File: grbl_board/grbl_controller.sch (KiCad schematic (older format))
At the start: 38 parts, among them J3 USB_B, J4 ICSP, SW1 SW_Push, U1 FT231XS, U2 ATmega2560-16AU, Y1 16M

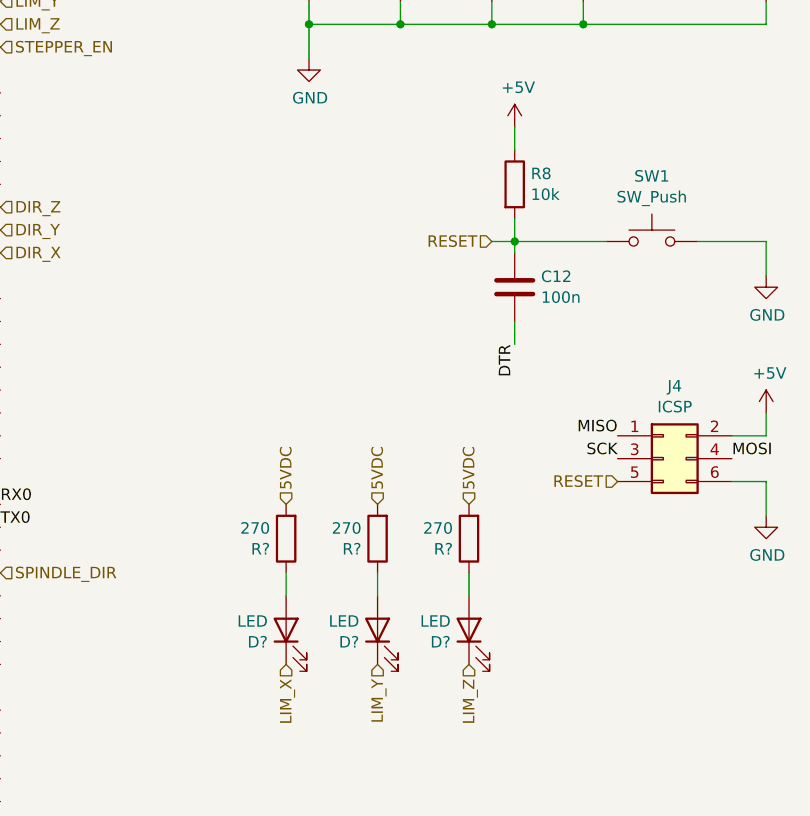
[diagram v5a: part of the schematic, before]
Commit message: updated board with 24V reg
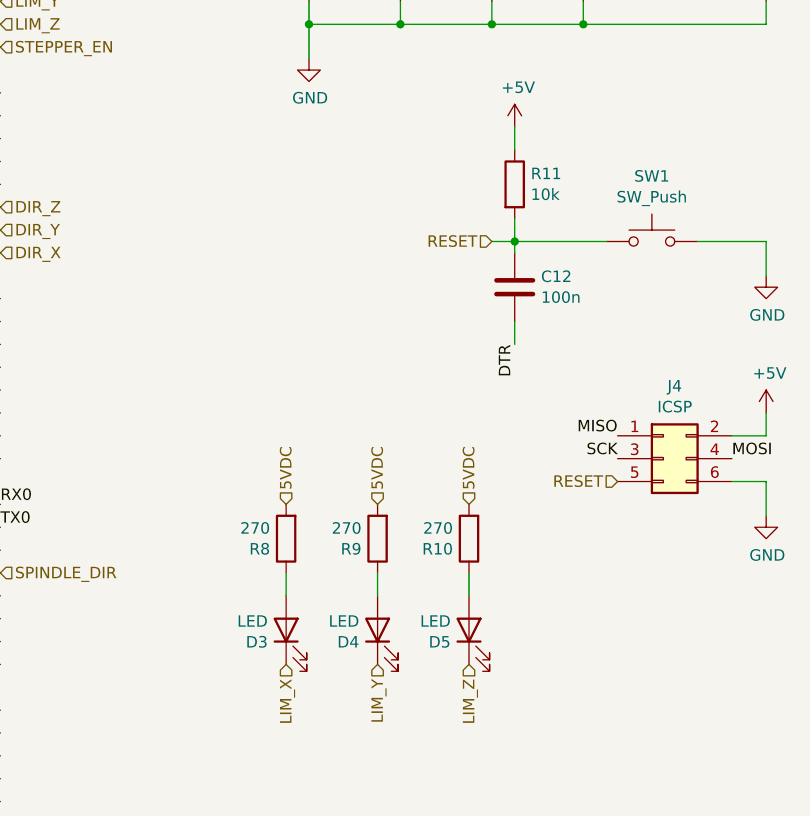
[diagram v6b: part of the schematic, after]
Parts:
- gave numbers to parts that had none: 6
- renumbered R8 to R11
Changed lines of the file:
@@
 $EndComp
 $Comp
-L power:GND #PWR09
+L power:GND #PWR011
 U 1 1 61772314
 P 3100 2100
-F 0 "#PWR09" H 3100 1850 50  0001 C CNN
+F 0 "#PWR011" H 3100 1850 50  0001 C CNN
 F 1 "GND" H 3105 1927 50  0000 C CNN
 F 2 "" H 3100 2100 50  0001 C CNN
@@
 	4700 2000 4700 2150
 $Comp
-L power:GND #PWR011
+L power:GND #PWR012
 U 1 1 6177BB8C
 P 4700 2550
-F 0 "#PWR011" H 4700 2300 50  0001 C CNN
+F 0 "#PWR012" H 4700 2300 50  0001 C CNN
 F 1 "GND" H 4705 2377 50  0000 C CNN
 F 2 "" H 4700 2550 50  0001 C CNN
@@
 	8500 2400 8900 2400
 $Comp
-L power:+5V #PWR014
+L power:+5V #PWR015
 U 1 1 617AAEC0
 P 8100 2300
-F 0 "#PWR014" H 8100 2150 50  0001 C CNN
+F 0 "#PWR015" H 8100 2150 50  0001 C CNN
 F 1 "+5V" H 8115 2473 50  0000 C CNN
 F 2 "" H 8100 2300 50  0001 C CNN
@@
 Connection ~ 8100 2400
 $Comp
-L power:GND #PWR015
+L power:GND #PWR016
 U 1 1 617AC8A9
 P 8100 3050
-F 0 "#PWR015" H 8100 2800 50  0001 C CNN
+F 0 "#PWR016" H 8100 2800 50  0001 C CNN
 F 1 "GND" H 8105 2877 50  0000 C CNN
 F 2 "" H 8100 3050 50  0001 C CNN
@@
 	6050 900  6050 1100
 $Comp
-L power:+5V #PWR012
+L power:+5V #PWR013
 U 1 1 617AFBE7
 P 5800 850
-F 0 "#PWR012" H 5800 700 50  0001 C CNN
+F 0 "#PWR013" H 5800 700 50  0001 C CNN
 F 1 "+5V" H 5815 1023 50  0000 C CNN
 F 2 "" H 5800 850 50  0001 C CNN
@@
 	5950 950  5950 1100
 $Comp
-L power:GND #PWR013
+L power:GND #PWR014
 U 1 1 617B278B
 P 5950 7100
-F 0 "#PWR013" H 5950 6850 50  0001 C CNN
+F 0 "#PWR014" H 5950 6850 50  0001 C CNN
 F 1 "GND" H 5955 6927 50  0000 C CNN
 F 2 "" H 5950 7100 50  0001 C CNN
@@
 SCK
 $Comp
-L power:GND #PWR017
+L power:GND #PWR018
 U 1 1 617C6BF5
 P 10100 4000
-F 0 "#PWR017" H 10100 3750 50  0001 C CNN
+F 0 "#PWR018" H 10100 3750 50  0001 C CNN
 F 1 "GND" H 10105 3827 50  0000 C CNN
 F 2 "" H 10100 4000 50  0001 C CNN
@@
 MISO
 $Comp
-L power:+5V #PWR018
+L power:+5V #PWR019
 U 1 1 617D7EA2
 P 10100 4600
-F 0 "#PWR018" H 10100 4450 50  0001 C CNN
+F 0 "#PWR019" H 10100 4450 50  0001 C CNN
 F 1 "+5V" H 10115 4773 50  0000 C CNN
 F 2 "" H 10100 4600 50  0001 C CNN
@@
 	10100 4700 9950 4700
 $Comp
-L power:GND #PWR019
+L power:GND #PWR020
 U 1 1 617D9FFF
 P 10100 5050
-F 0 "#PWR019" H 10100 4800 50  0001 C CNN
+F 0 "#PWR020" H 10100 4800 50  0001 C CNN
 F 1 "GND" H 10105 4877 50  0000 C CNN
 F 2 "" H 10100 5050 50  0001 C CNN
@@
 	3100 2000 3100 1700
 $Comp
-L power:+5V #PWR016
+L power:+5V #PWR017
 U 1 1 617EF684
 P 9000 3350
-F 0 "#PWR016" H 9000 3200 50  0001 C CNN
+F 0 "#PWR017" H 9000 3200 50  0001 C CNN
 F 1 "+5V" H 9015 3523 50  0000 C CNN
 F 2 "" H 9000 3350 50  0001 C CNN
@@
 	9000 3350 9000 3450
 $Comp
-L Device:R R8
+L Device:R R11
 U 1 1 617F074D
 P 9000 3600
-F 0 "R8" H 9070 3646 50  0000 L CNN
+F 0 "R11" H 9070 3646 50  0000 L CNN
 F 1 "10k" H 9070 3555 50  0000 L CNN
 F 2 "Resistor_SMD:R_0805_2012Metric_Pad1.15x1.40mm_HandSolder" V 8930 3600 50  0001 C CNN
@@
 	1550 6650 1550 6600
 $Comp
-L power:GND #PWR07
+L power:GND #PWR08
 U 1 1 61866176
 P 1150 6700
-F 0 "#PWR07" H 1150 6450 50  0001 C CNN
+F 0 "#PWR08" H 1150 6450 50  0001 C CNN
 F 1 "GND" H 1155 6527 50  0000 C CNN
 F 2 "" H 1150 6700 50  0001 C CNN
@@
 	1000 4550 1000 4400
 $Comp
-L power:GND #PWR06
+L power:GND #PWR07
 U 1 1 618A6872
 P 1000 4550
-F 0 "#PWR06" H 1000 4300 50  0001 C CNN
+F 0 "#PWR07" H 1000 4300 50  0001 C CNN
 F 1 "GND" H 1005 4377 50  0000 C CNN
 F 2 "" H 1000 4550 50  0001 C CNN
@@
 	1550 5850 1550 5900
 $Comp
-L power:GND #PWR08
+L power:GND #PWR09
 U 1 1 61898861
 P 1550 5900
-F 0 "#PWR08" H 1550 5650 50  0001 C CNN
+F 0 "#PWR09" H 1550 5650 50  0001 C CNN
 F 1 "GND" H 1555 5727 50  0000 C CNN
 F 2 "" H 1550 5900 50  0001 C CNN
@@
 AR Path="/619755E7/61CDF7A9" Ref="D?"  Part="1"
 AR Path="/61D39570/61CDF7A9" Ref="D?"  Part="1"
-F 0 "D?" V 8747 5630 50  0000 L CNN
+AR Path="/61764DEB/61CDF7A9" Ref="D5"  Part="1"
+F 0 "D5" V 8747 5630 50  0000 L CNN
 F 1 "LED" V 8838 5630 50  0000 L CNN
 F 2 "LED_SMD:LED_1206_3216Metric_Pad1.42x1.75mm_HandSolder" H 8800 5550 50  0001 C CNN
@@
 AR Path="/619755E7/61CDF7B0" Ref="R?"  Part="1"
 AR Path="/61D39570/61CDF7B0" Ref="R?"  Part="1"
-F 0 "R?" H 8870 5196 50  0000 L CNN
+AR Path="/61764DEB/61CDF7B0" Ref="R10"  Part="1"
+F 0 "R10" H 8870 5196 50  0000 L CNN
 F 1 "270" H 8870 5105 50  0000 L CNN
 F 2 "Resistor_SMD:R_0805_2012Metric_Pad1.15x1.40mm_HandSolder" V 8730 5150 50  0001 C CNN
@@
 AR Path="/619755E7/61CDF7B9" Ref="D?"  Part="1"
 AR Path="/61D39570/61CDF7B9" Ref="D?"  Part="1"
-F 0 "D?" V 8347 5630 50  0000 L CNN
+AR Path="/61764DEB/61CDF7B9" Ref="D4"  Part="1"
+F 0 "D4" V 8347 5630 50  0000 L CNN
 F 1 "LED" V 8438 5630 50  0000 L CNN
 F 2 "LED_SMD:LED_1206_3216Metric_Pad1.42x1.75mm_HandSolder" H 8400 5550 50  0001 C CNN
@@
 AR Path="/619755E7/61CDF7C0" Ref="R?"  Part="1"
 AR Path="/61D39570/61CDF7C0" Ref="R?"  Part="1"
-F 0 "R?" H 8470 5196 50  0000 L CNN
+AR Path="/61764DEB/61CDF7C0" Ref="R9"  Part="1"
+F 0 "R9" H 8470 5196 50  0000 L CNN
 F 1 "270" H 8470 5105 50  0000 L CNN
 F 2 "Resistor_SMD:R_0805_2012Metric_Pad1.15x1.40mm_HandSolder" V 8330 5150 50  0001 C CNN
@@
 AR Path="/619755E7/61CDF7C9" Ref="R?"  Part="1"
 AR Path="/61D39570/61CDF7C9" Ref="R?"  Part="1"
-F 0 "R?" H 8070 5196 50  0000 L CNN
+AR Path="/61764DEB/61CDF7C9" Ref="R8"  Part="1"
+F 0 "R8" H 8070 5196 50  0000 L CNN
 F 1 "270" H 8070 5105 50  0000 L CNN
 F 2 "Resistor_SMD:R_0805_2012Metric_Pad1.15x1.40mm_HandSolder" V 7930 5150 50  0001 C CNN
@@
 AR Path="/619755E7/61CDF7D0" Ref="D?"  Part="1"
 AR Path="/61D39570/61CDF7D0" Ref="D?"  Part="1"
-F 0 "D?" V 7947 5630 50  0000 L CNN
+AR Path="/61764DEB/61CDF7D0" Ref="D3"  Part="1"
+F 0 "D3" V 7947 5630 50  0000 L CNN
 F 1 "LED" V 8038 5630 50  0000 L CNN
 F 2 "LED_SMD:LED_1206_3216Metric_Pad1.42x1.75mm_HandSolder" H 8000 5550 50  0001 C CNN
